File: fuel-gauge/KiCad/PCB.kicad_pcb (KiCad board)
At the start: 2 copper layers, 100.1 x 70 mm, 39 parts, among them P1 CONN_01X04, P2 CONN_01X04, P3 CONN_01X04, Q1 BSS84, Q2 BSS138, Q3 2N7002, SW1 Switch_SPDT_x2, U1 AQV252G, U2 SN74LVC1G08DBVR, U3 TLV3691IDCKR, U4 bq34z100pw

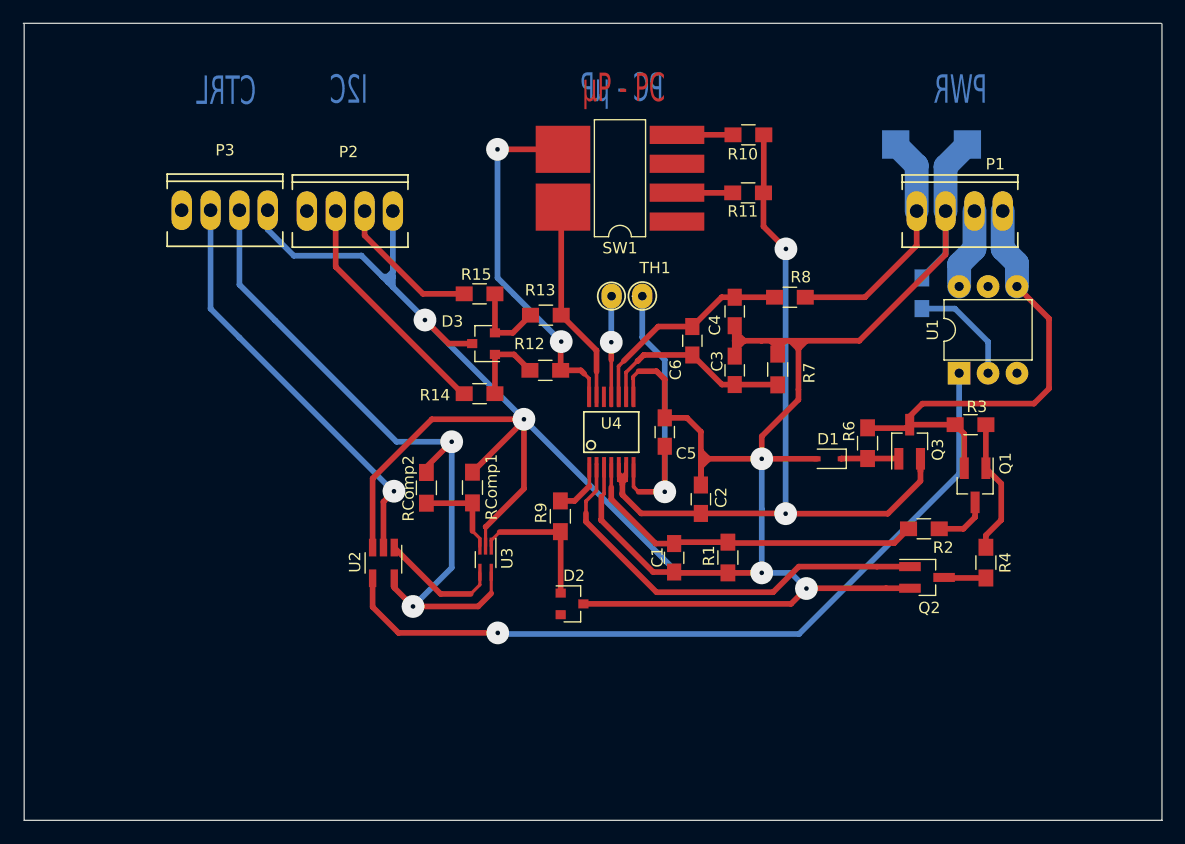
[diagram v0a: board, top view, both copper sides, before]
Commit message: Change a component and redesign drills
The thermistor is sustituted by a connector in order to have no wirings
in the PCB. The thermistor has to be located near the battery.

Drills were redesign in orther to create a correct version to send to a
PCB manufacturer.
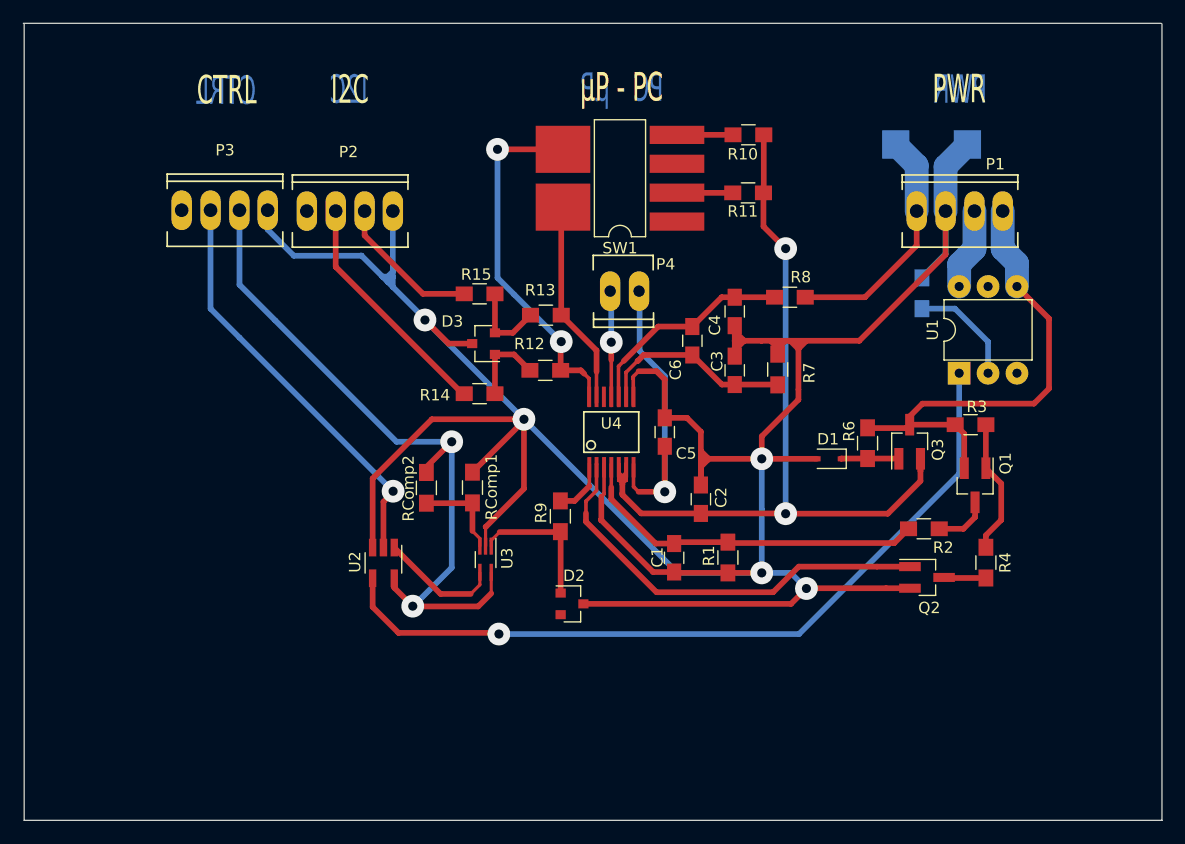
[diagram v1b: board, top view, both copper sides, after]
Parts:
- removed TH1: 10K, myfootprint:Thermistor
- added P4: CONN_01X02, footprint:CONN_01X02, F.Cu at (152.9, 83.4)
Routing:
- net REG_25: track 27.0 -> 27.5 mm

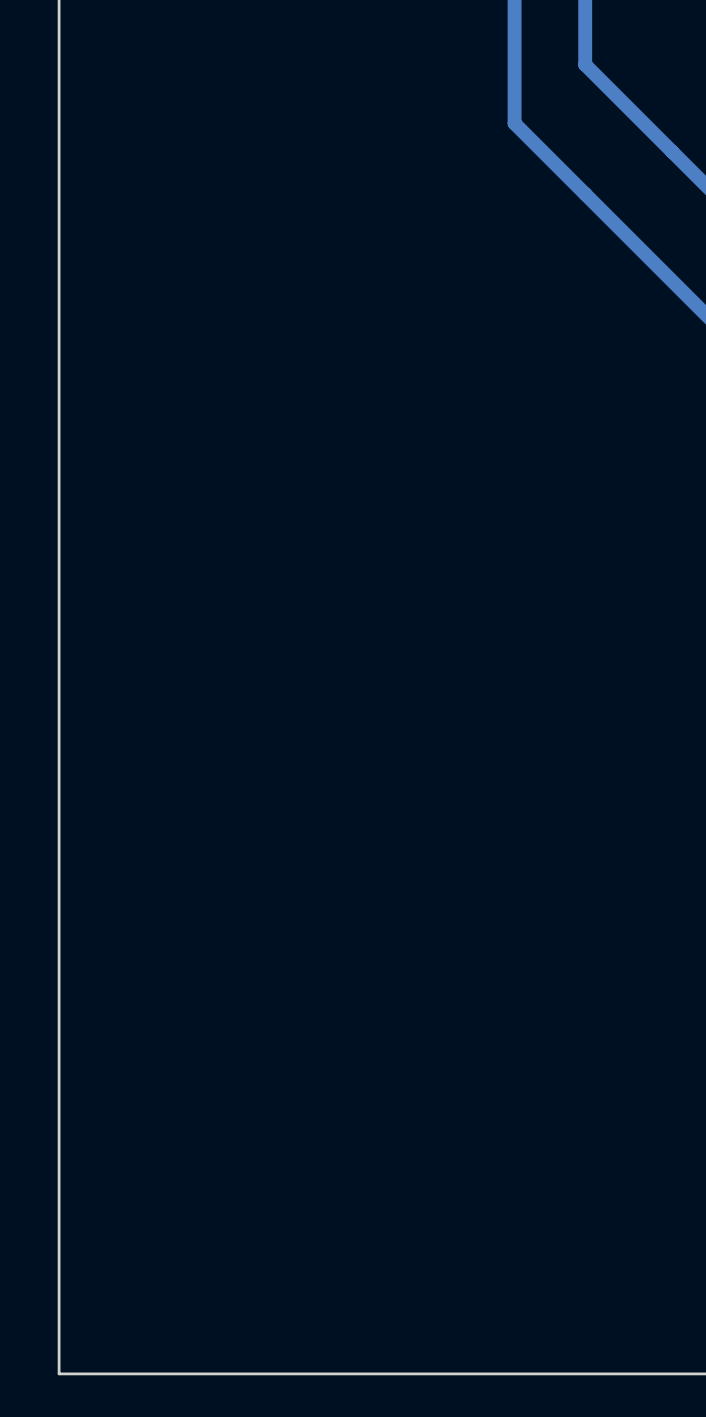
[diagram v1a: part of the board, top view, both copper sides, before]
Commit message: Update the v2.0 of the fuel gauge PCB
Include the Bill of Materials (BOM) with all the components

Include the new footprint of the mounting hole
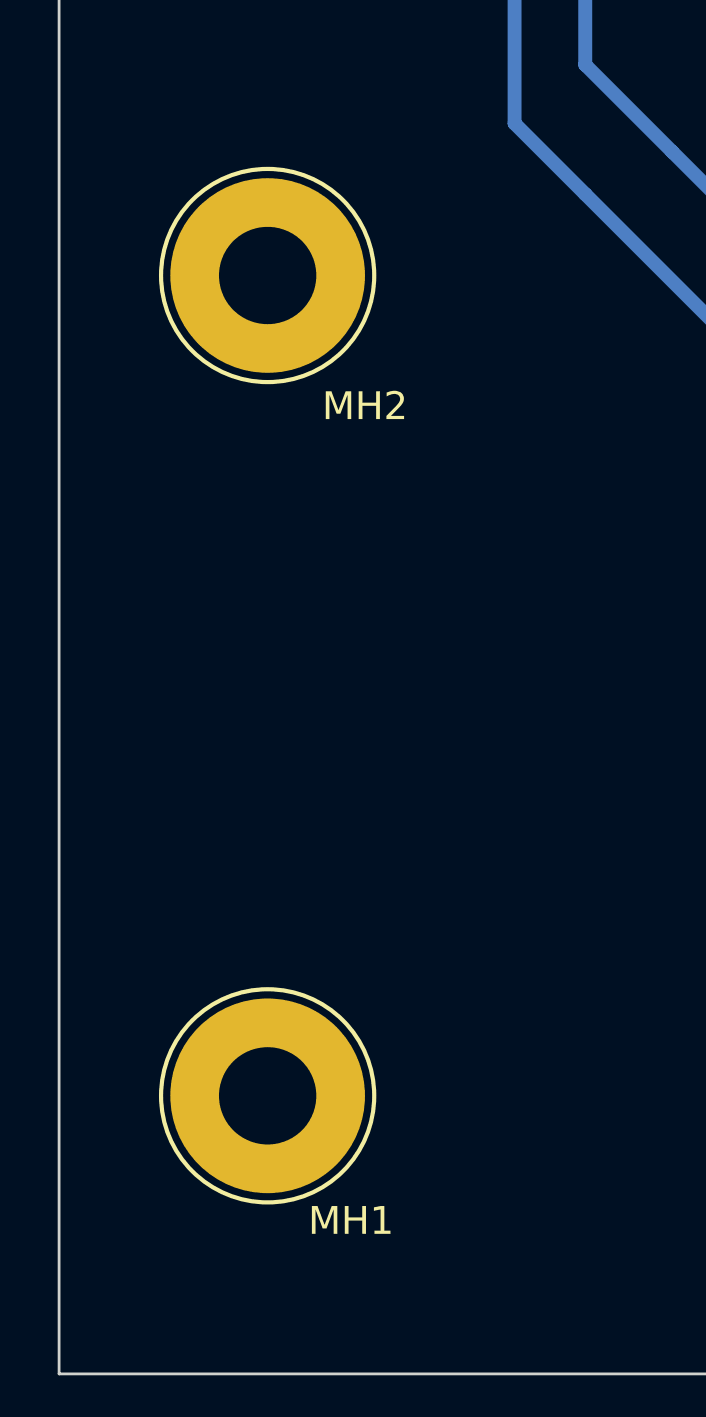
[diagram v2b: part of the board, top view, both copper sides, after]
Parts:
- added MH1: Mounting_Hole, footprint:Mounting_hole, F.Cu at (107.5, 120.0)
- added MH2: Mounting_Hole, footprint:Mounting_hole, F.Cu at (107.5, 90.5)
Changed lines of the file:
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@@
     (area 99.874999 59.899999 200.050001 130.050001)
     (thickness 1.6)
-    (drawings 27)
+    (drawings 31)
     (tracks 354)
     (zones 0)
-    (modules 39)
+    (modules 41)
     (nets 32)
   )
@@
     (pad_to_mask_clearance 0)
     (aux_axis_origin 0 0)
-    (visible_elements 7FFFEE69)
+    (visible_elements 7FFEFE69)
     (pcbplotparams
       (layerselection 0x00030_80000001)
@@
       (net 31 "Net-(P4-Pad2)"))
   )
+  (module footprint:Mounting_hole (layer F.Cu)
+    (at 107.5 120)
+    (descr "BNC connector")
+    (tags "BNC connector")
+    (fp_text reference MH1 (at 3 4.5) (layer F.SilkS)
+      (effects (font (size 1 1) (thickness 0.15)))
+    )
+    (fp_text value Mounting_Hole (at -0.2 5.9) (layer F.Fab)
+      (effects (font (size 1 1) (thickness 0.15)))
+    )
+    (fp_circle (center 0 0) (end 3.5 -1.9) (layer F.CrtYd) (width 0.15))
+    (fp_circle (center 0 0) (end 3.8 -0.5) (layer F.SilkS) (width 0.15))
+    (fp_circle (center 0 0) (end 3 -2.2) (layer F.Fab) (width 0.15))
+    (pad 1 thru_hole circle (at 0 0) (size 7 7) (drill 3.5) (layers *.Cu *.Mask))
+    (model Connectors.3dshapes\BNC.wrl
+      (at (xyz -0.5 0 0))
+      (scale (xyz 2 2 2))
+      (rotate (xyz 0 0 0))
+    )
+  )
+  (module footprint:Mounting_hole (layer F.Cu)
+    (at 107.5 90.5)
+    (descr "BNC connector")
+    (tags "BNC connector")
+    (fp_text reference MH2 (at 3.5 4.7) (layer F.SilkS)
+      (effects (font (size 1 1) (thickness 0.15)))
+    )
+    (fp_text value Mounting_Hole (at -0.2 5.9) (layer F.Fab)
+      (effects (font (size 1 1) (thickness 0.15)))
+    )
+    (fp_circle (center 0 0) (end 3.5 -1.9) (layer F.CrtYd) (width 0.15))
+    (fp_circle (center 0 0) (end 3.8 -0.5) (layer F.SilkS) (width 0.15))
+    (fp_circle (center 0 0) (end 3 -2.2) (layer F.Fab) (width 0.15))
+    (pad 1 thru_hole circle (at 0 0) (size 7 7) (drill 3.5) (layers *.Cu *.Mask))
+    (model Connectors.3dshapes\BNC.wrl
+      (at (xyz -0.5 0 0))
+      (scale (xyz 2 2 2))
+      (rotate (xyz 0 0 0))
+    )
+  )
+  (dimension 7.5 (width 0.3) (layer Margin)
+    (gr_text 7,500mm (at 103.75 101.35) (layer Margin)
+      (effects (font (size 1.5 1.5) (thickness 0.3)))
+    )
+    (feature1 (pts (xy 107.5 90.5) (xy 107.5 102.7)))
+    (feature2 (pts (xy 100 90.5) (xy 100 102.7)))
+    (crossbar (pts (xy 100 100) (xy 107.5 100)))
+    (arrow1a (pts (xy 107.5 100) (xy 106.373496 100.586421)))
+    (arrow1b (pts (xy 107.5 100) (xy 106.373496 99.413579)))
+    (arrow2a (pts (xy 100 100) (xy 101.126504 100.586421)))
+    (arrow2b (pts (xy 100 100) (xy 101.126504 99.413579)))
+  )
+  (dimension 29.5 (width 0.3) (layer Margin)
+    (gr_text 29,500mm (at 94.65 105.25 90) (layer Margin)
+      (effects (font (size 1.5 1.5) (thickness 0.3)))
+    )
+    (feature1 (pts (xy 100 90.5) (xy 93.3 90.5)))
+    (feature2 (pts (xy 100 120) (xy 93.3 120)))
+    (crossbar (pts (xy 96 120) (xy 96 90.5)))
+    (arrow1a (pts (xy 96 90.5) (xy 96.586421 91.626504)))
+    (arrow1b (pts (xy 96 90.5) (xy 95.413579 91.626504)))
+    (arrow2a (pts (xy 96 120) (xy 96.586421 118.873496)))
+    (arrow2b (pts (xy 96 120) (xy 95.413579 118.873496)))
+  )
+  (dimension 10 (width 0.3) (layer Margin)
+    (gr_text 10,000mm (at 94.65 125 270) (layer Margin)
+      (effects (font (size 1.5 1.5) (thickness 0.3)))
+    )
+    (feature1 (pts (xy 107.5 130) (xy 93.3 130)))
+    (feature2 (pts (xy 107.5 120) (xy 93.3 120)))
+    (crossbar (pts (xy 96 120) (xy 96 130)))
+    (arrow1a (pts (xy 96 130) (xy 95.413579 128.873496)))
+    (arrow1b (pts (xy 96 130) (xy 96.586421 128.873496)))
+    (arrow2a (pts (xy 96 120) (xy 95.413579 121.126504)))
+    (arrow2b (pts (xy 96 120) (xy 96.586421 121.126504)))
+  )
+  (dimension 7.5 (width 0.3) (layer Margin)
+    (gr_text 7,500mm (at 103.75 133.85) (layer Margin)
+      (effects (font (size 1.5 1.5) (thickness 0.3)))
+    )
+    (feature1 (pts (xy 100 120) (xy 100 135.2)))
+    (feature2 (pts (xy 107.5 120) (xy 107.5 135.2)))
+    (crossbar (pts (xy 107.5 132.5) (xy 100 132.5)))
+    (arrow1a (pts (xy 100 132.5) (xy 101.126504 131.913579)))
+    (arrow1b (pts (xy 100 132.5) (xy 101.126504 133.086421)))
+    (arrow2a (pts (xy 107.5 132.5) (xy 106.373496 131.913579)))
+    (arrow2b (pts (xy 107.5 132.5) (xy 106.373496 133.086421)))
+  )
   (gr_text CTRL (at 117.8 65.825) (layer F.SilkS)
     (effects (font (size 2.5 1.5) (thickness 0.375)))
@@
   (target plus (at 195 65) (size 5) (width 0.1) (layer Edge.Cuts))
   (target plus (at 105 65) (size 5) (width 0.1) (layer Edge.Cuts))
-  (target plus (at 105 125) (size 5) (width 0.1) (layer Edge.Cuts))
+  (target plus (at 103 127) (size 5) (width 0.1) (layer Edge.Cuts))
   (target plus (at 195 125) (size 5) (width 0.1) (layer Edge.Cuts))
   (dimension 10 (width 0.3) (layer Margin)
@@
   (segment (start 162.45 84.025) (end 165.95 84.025) (width 0.5) (layer F.Cu) (net 4))
   (segment (start 162.45 84.025) (end 161.3 84.025) (width 0.5) (layer F.Cu) (net 4))
-  (segment (start 154.093 83.5385) (end 154.093 88.743) (width 0.5) (layer B.Cu) (net 5) (status 400000))
+  (segment (start 154.093 83.5385) (end 154.093 88.743) (width 0.5) (layer B.Cu) (net 5))
   (segment (start 156.3 90.95) (end 154.093 88.743) (width 0.5) (layer B.Cu) (net 5))
   (via (at 156.3 101.125) (size 2) (drill 0.8) (layers F.Cu B.Cu) (net 5))
   (segment (start 156.3 90.95) (end 156.3 101.125) (width 0.5) (layer B.Cu) (net 5))
-  (segment (start 154.093 83.5385) (end 154.043 83.4885) (width 0.5) (layer B.Cu) (net 5) (status C00000))
+  (segment (start 154.093 83.5385) (end 154.043 83.4885) (width 0.5) (layer B.Cu) (net 5))
   (segment (start 156.3 97.125) (end 156.3 101.125) (width 0.5) (layer F.Cu) (net 5))
   (segment (start 153.5558 100.6808) (end 154 101.125) (width 0.32) (layer F.Cu) (net 5))
@@
   (segment (start 131.575 102) (end 132.5 101.075) (width 0.5) (layer F.Cu) (net 30))
   (segment (start 132.5 101.075) (end 132.425 101.075) (width 0.5) (layer B.Cu) (net 30))
-  (segment (start 151.6 83.5855) (end 151.6 87.975) (width 0.5) (layer B.Cu) (net 31) (status 400000))
+  (segment (start 151.6 83.5855) (end 151.6 87.975) (width 0.5) (layer B.Cu) (net 31))
   (via (at 151.6 87.975) (size 2) (drill 0.8) (layers F.Cu B.Cu) (net 31))
   (segment (start 151.6 89.525) (end 151.6 93.531) (width 0.32) (layer F.Cu) (net 31))
   (segment (start 151.6 89.525) (end 151.6 87.975) (width 0.5) (layer F.Cu) (net 31))
-  (segment (start 151.6 83.5855) (end 151.503 83.4885) (width 0.5) (layer B.Cu) (net 31) (status C00000))
+  (segment (start 151.6 83.5855) (end 151.503 83.4885) (width 0.5) (layer B.Cu) (net 31))
 )

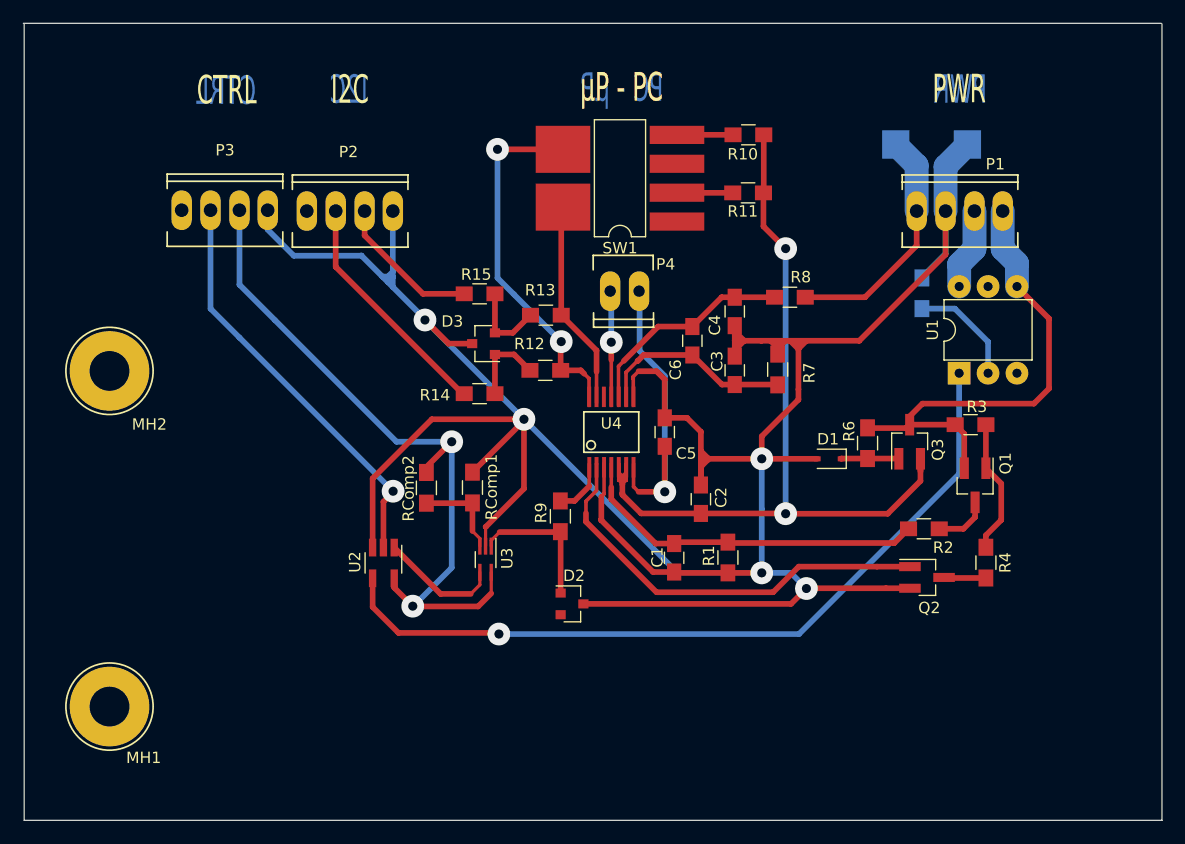
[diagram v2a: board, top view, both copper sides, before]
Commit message: Prepare Silk Layer in order to be able to manufacture
This 'manu2' branch was created in order to have the 3 projects
on the same folder.

The silk layer was created and adapted to give it to an external
manufacturer.
Nearly the same information was created in the copper layer in order to
have this information also in the case the PCB's were manufactured in
the DTE.
The Mask layer was also adapted to give it to the external manufacturer.
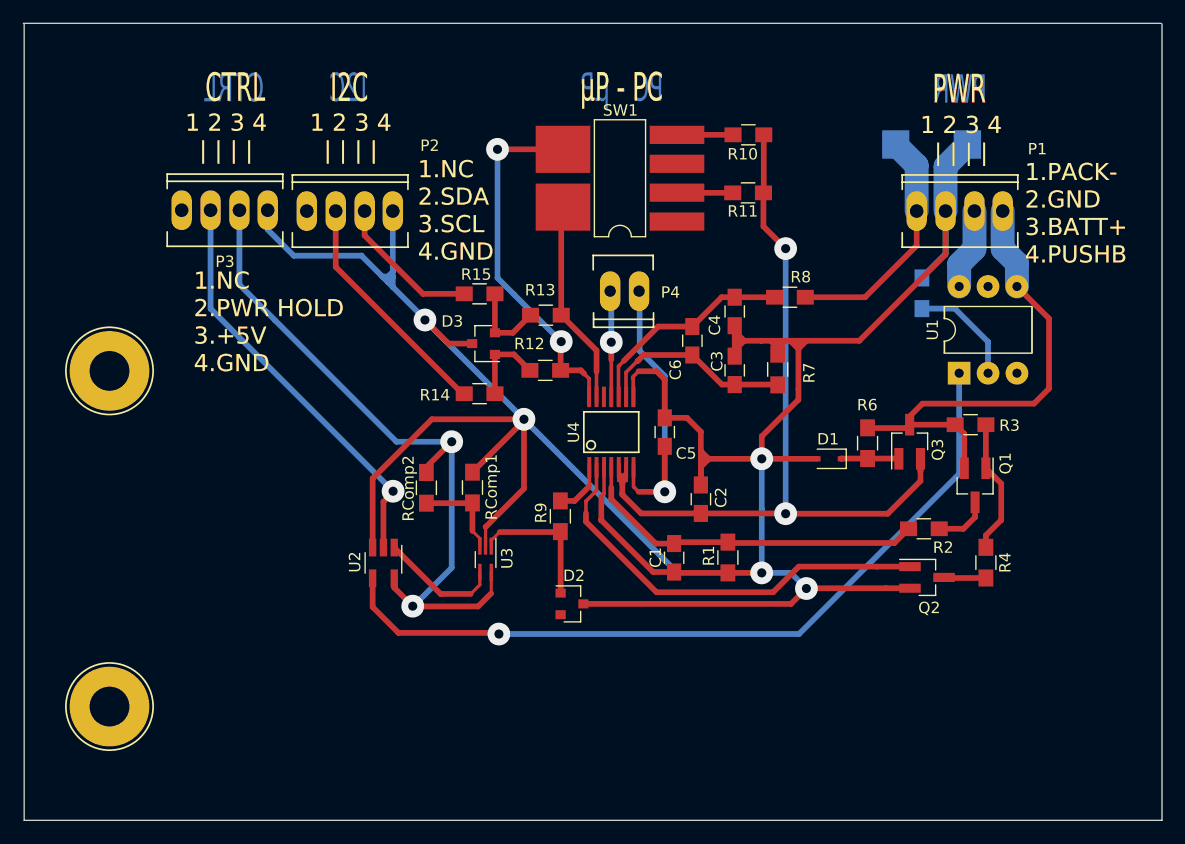
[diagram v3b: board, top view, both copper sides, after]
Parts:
- U1: footprint footprint:DIP-6_W7.62mm -> DIP-6_W7.62mm
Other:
- rule pad_to_mask_clearance: 0 -> 0.1
- board text added: "1 2 3 4 | | | |"
- board text added: "1.NC 2.PWR HOLD 3.+5V 4.GND"
- board text added: "1.NC 2.SDA 3.SCL 4.GND"
- board text added: "1.PACK- 2.GND 3.BATT+ 4.PUSHB"
